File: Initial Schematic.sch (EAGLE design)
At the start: 8 parts, among them IC1 AD820R, J1 CONNECTOR, U1 CAN_TRANSCAN_TRANS, U2 3V3->5V_VREG

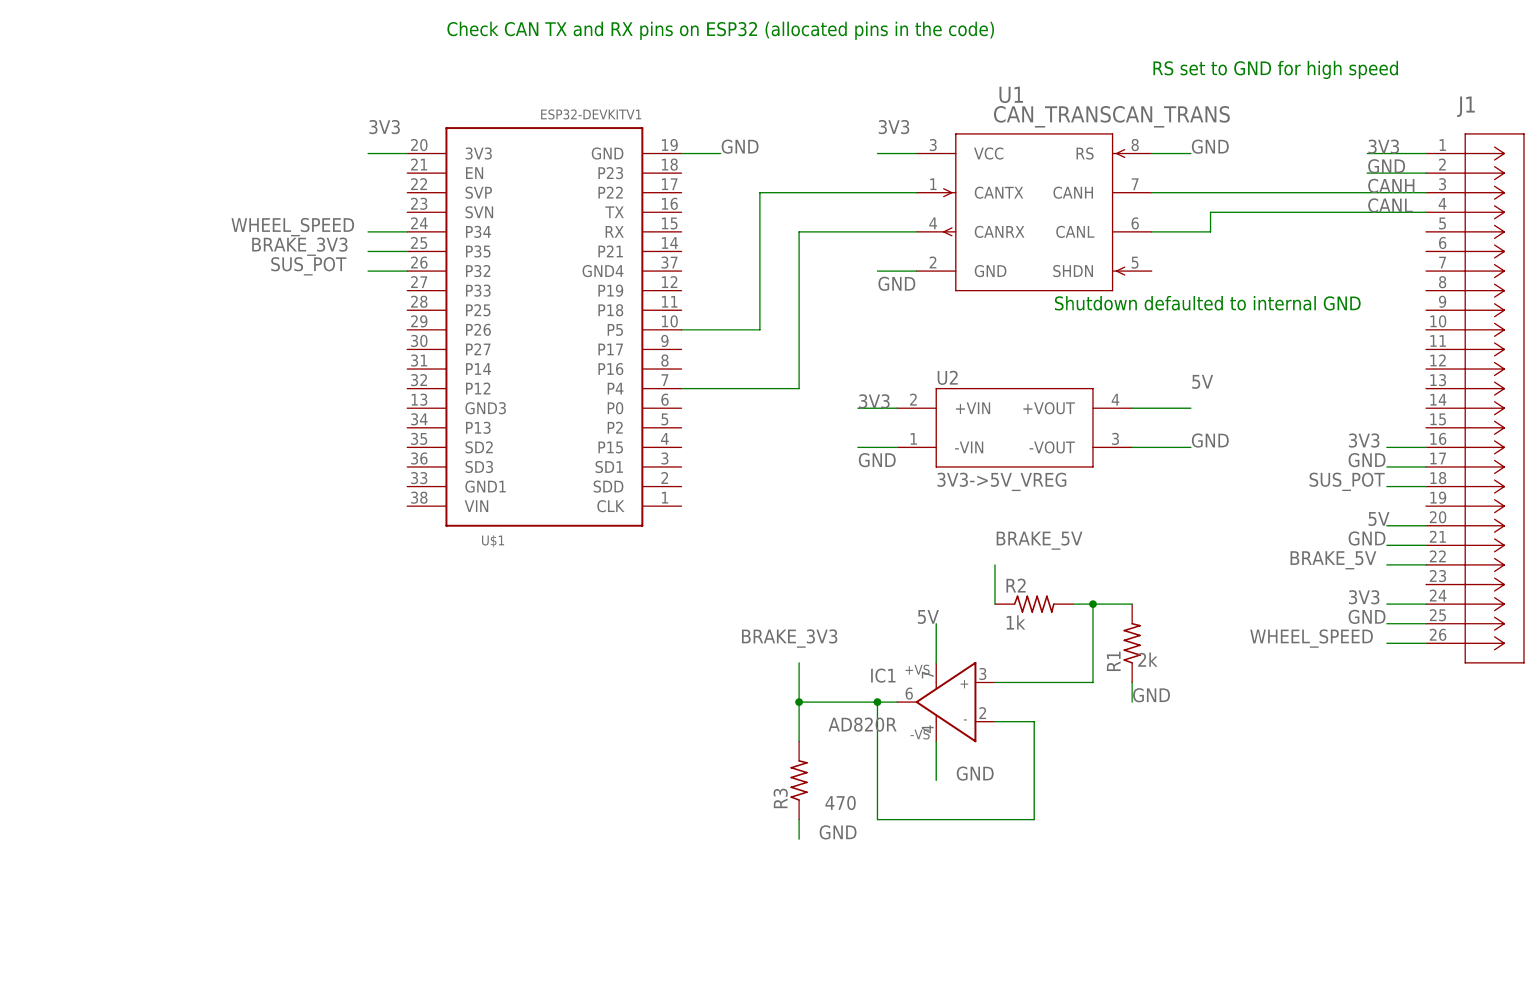
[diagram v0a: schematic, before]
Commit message: Removed Boost
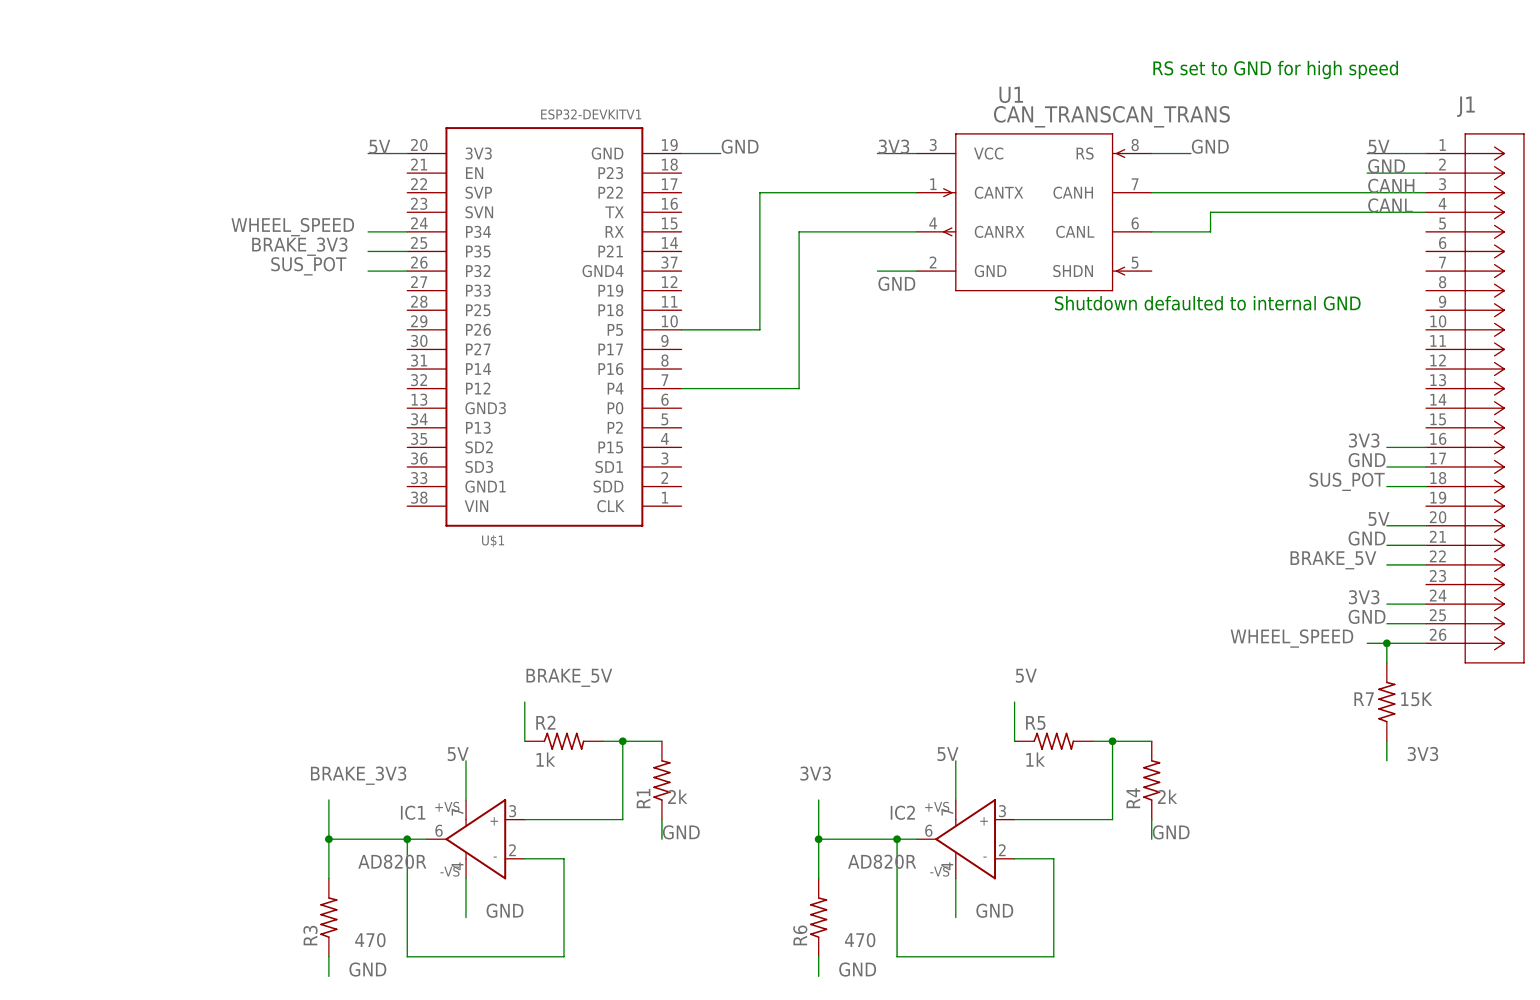
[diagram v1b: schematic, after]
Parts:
- removed U2: 3V3->5V_VREG, NFR23:3V3->5V_VREG
- added IC2: AD820R, analog-devices:AD820R
- added R4: 2k, NFR23:RESISTORR0603
- added R5: 1k, NFR23:RESISTORR0603
- added R6: 470, NFR23:RESISTORR0603
- added R7: 15K, NFR23:RESISTORR0603
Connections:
- new net N$4: IC2.IN+, R4.2, R5.2
- net 3V3: now also IC2.IN-, IC2.OUT, R6.2, R7.1; no longer J1.1, U$1.3V3, U2.+VIN
- net 5V: now also IC2.+VS, J1.1, R5.1, U$1.3V3; no longer U2.+VOUT
- net GND: now also IC2.-VS, R4.1, R6.1; no longer U2.-VIN, U2.-VOUT
- net WHEEL_SPEED: now also R7.2
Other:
- note removed: "Check CAN TX and RX pins on ESP32 (allocated pins in the code)"
- moved on the sheet: IC1, R1, R2, R3

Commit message: Created PCB Layout
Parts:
- removed IC1, IC2: AD820R, analog-devices:AD820R
- removed R3, R6: 470, NFR23:RESISTORR0603
- removed R4: 2k, NFR23:RESISTORR0603
- removed R5: 1k, NFR23:RESISTORR0603
- removed R7: 15K, NFR23:RESISTORR0603
- added C1, C2: 1.0µF, NFR23:CAPACITORC0603
- added LD1, LD2: PL006-WCR21, led:PL006-WCR21
- added U2: XC6210B332MR-G, CX6210B332MR-G:XC6210B332MR-G
- R1: value 2k -> 330
- R2: value 1k -> 330
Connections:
- removed net SUS_POT: J1.18, U$1.P32
- new net CAN_SHDN: U$1.P25, U1.SHDN
- new net N$5: LD2.C, R2.2
- net 3V3: now also J1.5, U$1.3V3; no longer IC2.IN-, IC2.OUT, J1.16, J1.24, R6.2, R7.1
- net 5V: now also J1.6, LD1.C, R1.1, U$1.VIN; no longer IC1.+VS, IC2.+VS, J1.20, R5.1, U$1.3V3
- net BRAKE_3V3: now also C2.1, U2.VOUT; no longer IC1.IN-, IC1.OUT, R3.2
- net BRAKE_5V: now also C1.1, J1.7, U2.CE, U2.VIN; no longer J1.22, R2.1
- net CANH: now also J1.4; no longer J1.3
- net CANL: now also J1.3; no longer J1.4
- net GND: now also C1.2, C2.2, J1.9, R2.1, U2.VSS; no longer IC1.-VS, IC2.-VS, J1.17, J1.21, J1.25, R1.1, R3.1, R4.1, R6.1
- net N$2: now also LD1.A; no longer IC1.IN+, R2.2
- net N$4: now also LD2.A, U$1.P33; no longer IC2.IN+, R4.2, R5.2
- net WHEEL_SPEED: now also J1.8; no longer J1.26, R7.2
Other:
- moved on the sheet: R1, R2

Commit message: Revised layout
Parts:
- removed C1, C2: 1.0µF, NFR23:CAPACITORC0603
- removed U2: XC6210B332MR-G, CX6210B332MR-G:XC6210B332MR-G
- added R3: 1k, NFR23:RESISTORR0603
- added R4: 2k, NFR23:RESISTORR0603
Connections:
- net 5V: no longer LD1.C
- net BRAKE_3V3: now also R3.1, R4.2; no longer C2.1, U2.VOUT
- net BRAKE_5V: now also R3.2; no longer C1.1, U2.CE, U2.VIN
- net GND: now also LD1.C, R4.1; no longer C1.2, C2.2, U2.VSS
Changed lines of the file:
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@@
 </class>
 </classes>
-<groups>
-<schematic_group name="REGULATOR"/>
-</groups>
 <parts>
 <part name="U$1" library="NFR23" deviceset="ESP32DEVKITV1" device=""/>
 <part name="J1" library="NFR23" deviceset="CONNECTOR" device=""/>
 <part name="U1" library="NFR23" deviceset="CAN_TRANS" device="CAN_TRANS"/>
-<part name="U2" library="CX6210B332MR-G" deviceset="XC6210B332MR-G" device=""/>
-<part name="C1" library="NFR23" deviceset="CAPACITOR" device="C0603" package3d_urn="urn:adsk.eagle:package:23616/2" value="1.0µF"/>
-<part name="C2" library="NFR23" deviceset="CAPACITOR" device="C0603" package3d_urn="urn:adsk.eagle:package:23616/2" value="1.0µF"/>
 <part name="LD1" library="led" library_urn="urn:adsk.eagle:library:259" deviceset="PL006*" device="-WCR21" package3d_urn="urn:adsk.eagle:package:28738/2"/>
 <part name="R1" library="NFR23" deviceset="RESISTOR" device="R0603" package3d_urn="urn:adsk.eagle:package:23555/3" value="330"/>
 <part name="LD2" library="led" library_urn="urn:adsk.eagle:library:259" deviceset="PL006*" device="-WCR21" package3d_urn="urn:adsk.eagle:package:28738/2"/>
 <part name="R2" library="NFR23" deviceset="RESISTOR" device="R0603" package3d_urn="urn:adsk.eagle:package:23555/3" value="330"/>
+<part name="R3" library="NFR23" deviceset="RESISTOR" device="R0603" package3d_urn="urn:adsk.eagle:package:23555/3" value="1k"/>
+<part name="R4" library="NFR23" deviceset="RESISTOR" device="R0603" package3d_urn="urn:adsk.eagle:package:23555/3" value="2k"/>
 </parts>
 <sheets>
@@
 <attribute name="VALUE" x="73.3806" y="54.8386" size="2.0828" layer="96" ratio="6" rot="SR0"/>
 </instance>
-<instance part="U2" gate="A" x="30.48" y="-17.78" smashed="yes" grouprefs="REGULATOR">
-<attribute name="VALUE" x="45.4406" y="-11.2014" size="2.0828" layer="96" ratio="6" rot="SR0"/>
-</instance>
-<instance part="C1" gate="G$1" x="20.32" y="-35.56" smashed="yes" grouprefs="REGULATOR">
-<attribute name="NAME" x="21.844" y="-35.179" size="1.778" layer="95"/>
-<attribute name="VALUE" x="21.844" y="-40.259" size="1.778" layer="96"/>
-</instance>
-<instance part="C2" gate="G$1" x="76.2" y="-27.94" smashed="yes" grouprefs="REGULATOR">
-<attribute name="NAME" x="77.724" y="-27.559" size="1.778" layer="95"/>
-<attribute name="VALUE" x="77.724" y="-32.639" size="1.778" layer="96"/>
-</instance>
 <instance part="LD1" gate="G$1" x="-15.24" y="-2.54" smashed="yes" rot="R90">
 <attribute name="NAME" x="-10.668" y="1.016" size="1.778" layer="95" rot="R180"/>
@@
 <attribute name="NAME" x="-44.45" y="34.5186" size="1.778" layer="95"/>
 <attribute name="VALUE" x="-44.45" y="29.718" size="1.778" layer="96"/>
+</instance>
+<instance part="R3" gate="G$1" x="88.9" y="10.16" smashed="yes">
+<attribute name="NAME" x="85.09" y="11.6586" size="1.778" layer="95"/>
+<attribute name="VALUE" x="85.09" y="6.858" size="1.778" layer="96"/>
+</instance>
+<instance part="R4" gate="G$1" x="71.12" y="10.16" smashed="yes">
+<attribute name="NAME" x="67.31" y="11.6586" size="1.778" layer="95"/>
+<attribute name="VALUE" x="67.31" y="6.858" size="1.778" layer="96"/>
 </instance>
 </instances>
@@
 </segment>
 <segment>
-<wire x1="20.32" y1="-40.64" x2="20.32" y2="-45.72" width="0.1524" layer="91" grouprefs="REGULATOR"/>
-<pinref part="C1" gate="G$1" pin="2"/>
-<label x="20.32" y="-48.26" size="1.778" layer="95" grouprefs="REGULATOR"/>
-</segment>
-<segment>
-<pinref part="U2" gate="A" pin="VSS"/>
-<wire x1="50.8" y1="-43.18" x2="50.8" y2="-38.1" width="0.1524" layer="91" grouprefs="REGULATOR"/>
-<label x="50.8" y="-45.72" size="1.778" layer="95" grouprefs="REGULATOR"/>
-</segment>
-<segment>
-<pinref part="C2" gate="G$1" pin="2"/>
-<wire x1="76.2" y1="-33.02" x2="76.2" y2="-38.1" width="0.1524" layer="91" grouprefs="REGULATOR"/>
-<label x="76.2" y="-40.64" size="1.778" layer="95" grouprefs="REGULATOR"/>
-</segment>
-<segment>
 <pinref part="R2" gate="G$1" pin="1"/>
 <wire x1="-45.72" y1="33.02" x2="-50.8" y2="33.02" width="0.1524" layer="91"/>
@@
 <wire x1="129.54" y1="30.48" x2="127" y2="30.48" width="0.1524" layer="91"/>
 <label x="121.92" y="30.48" size="1.778" layer="95"/>
+</segment>
+<segment>
+<pinref part="LD1" gate="G$1" pin="C"/>
+<wire x1="-10.16" y1="-2.54" x2="-7.62" y2="-2.54" width="0.1524" layer="91"/>
+<label x="-7.62" y="-2.54" size="1.778" layer="95"/>
+</segment>
+<segment>
+<pinref part="R4" gate="G$1" pin="1"/>
+<wire x1="66.04" y1="10.16" x2="60.96" y2="10.16" width="0.1524" layer="91"/>
+<label x="58.42" y="7.62" size="1.778" layer="95"/>
 </segment>
 </net>
@@
 <wire x1="-33.02" y1="-2.54" x2="-33.02" y2="5.08" width="0.1524" layer="91"/>
 <pinref part="U$1" gate="G$1" pin="VIN"/>
-<wire x1="-33.02" y1="5.08" x2="-7.62" y2="5.08" width="0.1524" layer="91"/>
-<pinref part="LD1" gate="G$1" pin="C"/>
-<wire x1="-7.62" y1="5.08" x2="-2.54" y2="5.08" width="0.1524" layer="91"/>
-<wire x1="-10.16" y1="-2.54" x2="-7.62" y2="-2.54" width="0.1524" layer="91"/>
-<wire x1="-7.62" y1="-2.54" x2="-7.62" y2="5.08" width="0.1524" layer="91"/>
-<junction x="-7.62" y="5.08"/>
+<wire x1="-33.02" y1="5.08" x2="-2.54" y2="5.08" width="0.1524" layer="91"/>
 <wire x1="-33.02" y1="5.08" x2="-38.1" y2="5.08" width="0.1524" layer="91"/>
 <junction x="-33.02" y="5.08"/>
@@
 </segment>
 <segment>
-<pinref part="U2" gate="A" pin="VOUT"/>
-<wire x1="68.58" y1="-17.78" x2="76.2" y2="-17.78" width="0.1524" layer="91" grouprefs="REGULATOR"/>
-<wire x1="76.2" y1="-17.78" x2="86.36" y2="-17.78" width="0.1524" layer="91" grouprefs="REGULATOR"/>
-<wire x1="76.2" y1="-17.78" x2="76.2" y2="-25.4" width="0.1524" layer="91" grouprefs="REGULATOR"/>
-<junction x="76.2" y="-17.78" grouprefs="REGULATOR"/>
-<pinref part="C2" gate="G$1" pin="1"/>
-<label x="81.28" y="-20.32" size="1.778" layer="95" grouprefs="REGULATOR"/>
+<pinref part="R4" gate="G$1" pin="2"/>
+<pinref part="R3" gate="G$1" pin="1"/>
+<wire x1="76.2" y1="10.16" x2="81.28" y2="10.16" width="0.1524" layer="91"/>
+<wire x1="81.28" y1="10.16" x2="83.82" y2="10.16" width="0.1524" layer="91"/>
+<wire x1="81.28" y1="10.16" x2="81.28" y2="-2.54" width="0.1524" layer="91"/>
+<junction x="81.28" y="10.16"/>
+<label x="81.28" y="-5.08" size="1.778" layer="95"/>
 </segment>
 </net>
 <net name="BRAKE_5V" class="0">
-<segment>
-<pinref part="U2" gate="A" pin="CE"/>
-<wire x1="33.02" y1="-25.4" x2="27.94" y2="-25.4" width="0.1524" layer="91" grouprefs="REGULATOR"/>
-<pinref part="U2" gate="A" pin="VIN"/>
-<wire x1="27.94" y1="-25.4" x2="20.32" y2="-25.4" width="0.1524" layer="91" grouprefs="REGULATOR"/>
-<wire x1="33.02" y1="-17.78" x2="27.94" y2="-17.78" width="0.1524" layer="91" grouprefs="REGULATOR"/>
-<wire x1="27.94" y1="-17.78" x2="27.94" y2="-25.4" width="0.1524" layer="91" grouprefs="REGULATOR"/>
-<junction x="27.94" y="-25.4" grouprefs="REGULATOR"/>
-<wire x1="20.32" y1="-25.4" x2="20.32" y2="-33.02" width="0.1524" layer="91" grouprefs="REGULATOR"/>
-<pinref part="C1" gate="G$1" pin="1"/>
-<wire x1="20.32" y1="-25.4" x2="12.7" y2="-25.4" width="0.1524" layer="91" grouprefs="REGULATOR"/>
-<junction x="20.32" y="-25.4" grouprefs="REGULATOR"/>
-<label x="2.54" y="-25.4" size="1.778" layer="95" grouprefs="REGULATOR"/>
-</segment>
 <segment>
 <pinref part="J1" gate="A" pin="7"/>
 <wire x1="129.54" y1="35.56" x2="127" y2="35.56" width="0.1524" layer="91"/>
 <label x="116.84" y="35.56" size="1.778" layer="95"/>
+</segment>
+<segment>
+<wire x1="101.6" y1="10.16" x2="93.98" y2="10.16" width="0.1524" layer="91"/>
+<pinref part="R3" gate="G$1" pin="2"/>
+<label x="101.6" y="10.16" size="1.778" layer="95"/>
 </segment>
 </net>
@@
 packages will not be understood (or retained) with this version.
 </note>
-<note version="9.5" severity="warning">
-Since Version 9.5, EAGLE supports persistent groups with
-schematics, and board files. Those persistent groups
-will not be understood (or retained) with this version.
-</note>
 <note version="8.4" severity="warning">
